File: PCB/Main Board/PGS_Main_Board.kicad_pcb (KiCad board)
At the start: 4 copper layers, 109.9 x 60.8 mm, 119 parts, among them J1 SM02B-SURS-TF_LF__SN_, J2 SM02B-SURS-TF_LF__SN_, J3 Molex 505110-0892, J5 Molex 505110-0892, J6 Molex 505110-0492, J7 Molex 505110-0492, J8 Conn_01x04_Pin, J9 Molex 505110-1792, Q1 MMBT2222A, Q2 MMBT2222A, SW1 TS-1187A-C-A-B, SW10 SW_Push, SW11 SW_Push, SW12 SW_Push, SW13 SW_Push, SW14 EVQ-P0E07K, SW15 1TS026A-1000-0550, SW16 TS-1187A-C-A-B, SW2 TS-1187A-C-A-B, SW3 TS-1187A-C-A-B, SW4 TS-1187A-C-A-B, SW5 SW_Push, SW6 SW_Push, SW7 SW_Push, SW8 SW_Push, SW9 EVQ-P0E07K, U1 RP2040, U3 GD25Q80EEIGR, U4 ST_LSM6, U5 ST_LSM6, Y1 ABM8-272-T3

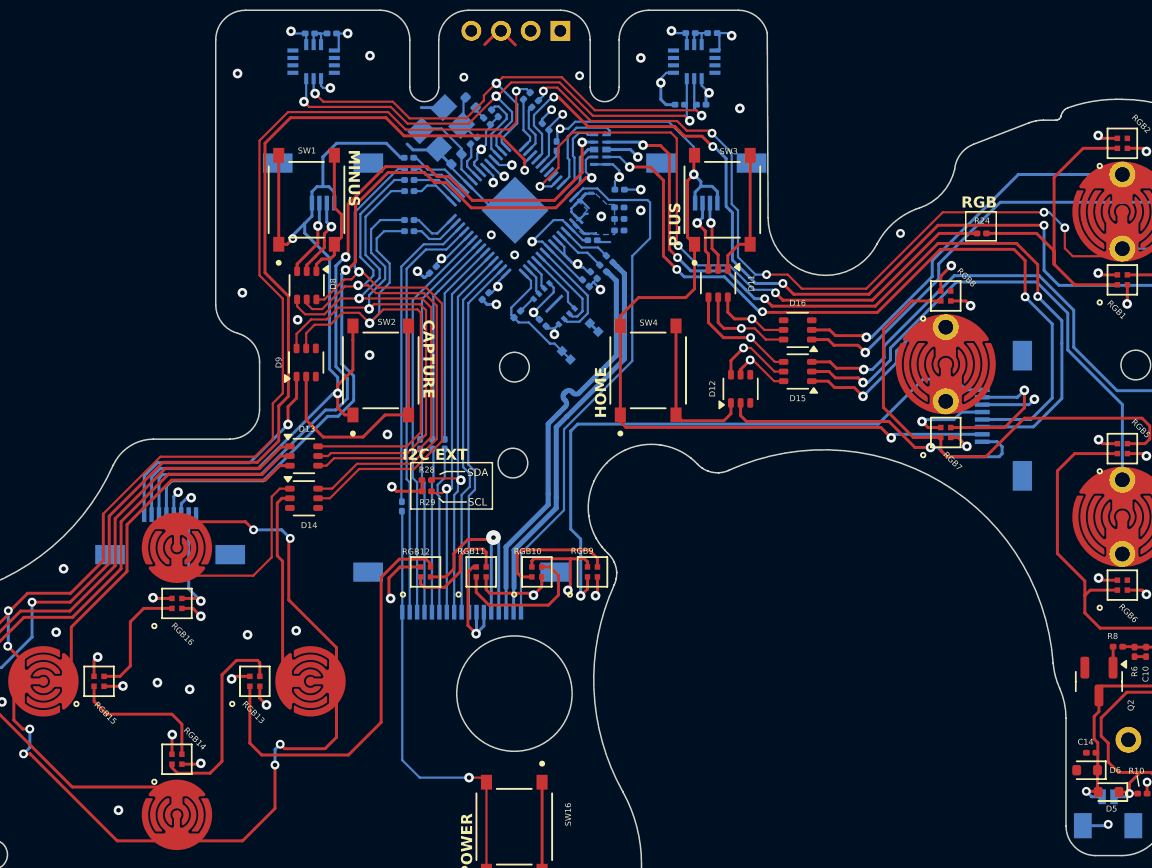
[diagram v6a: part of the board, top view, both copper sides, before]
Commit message: Final Routing 3D Export
- Export 3D STEP models
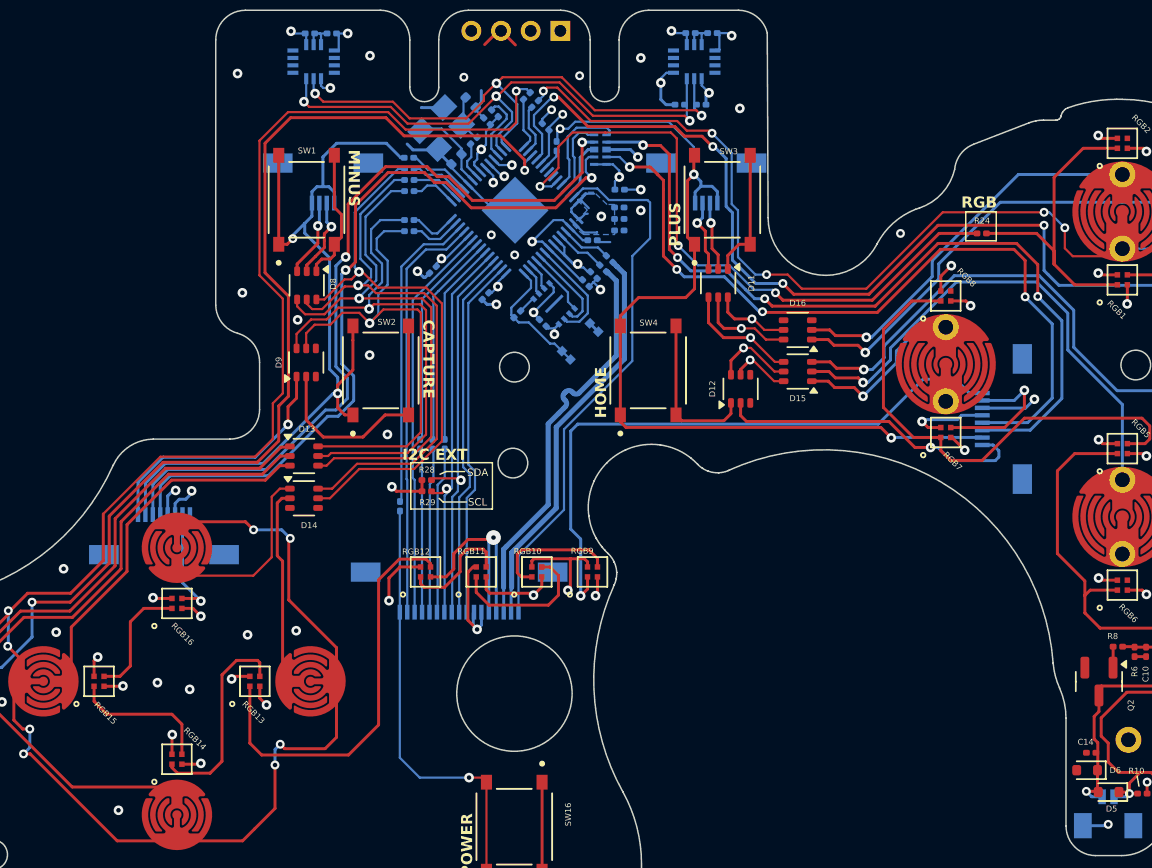
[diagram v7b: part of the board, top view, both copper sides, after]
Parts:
- moved J5 0.41 mm to (47.2, 49.9)
- moved J3 0.22 mm to (104.9, 40.9)
- moved J9 0.17 mm to (67.1, 51.5)
- moved R30 0.13 mm to (63.1, 46.8)
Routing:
- net +3V3: track 94.8 -> 95.7 mm
- net GND: track 91.5 -> 92.2 mm
